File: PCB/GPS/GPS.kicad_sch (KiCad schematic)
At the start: 33 parts, among them J1 DC, J2 USB-C, J3 Shelly, J4 Conn_01x05_Male, J5 Conn_01x05_Male, U1 L86-M33, U2 ESP32-PICO-MINI-02, U3 FT231XQ, U4 LMR16006+FB, U5 QR

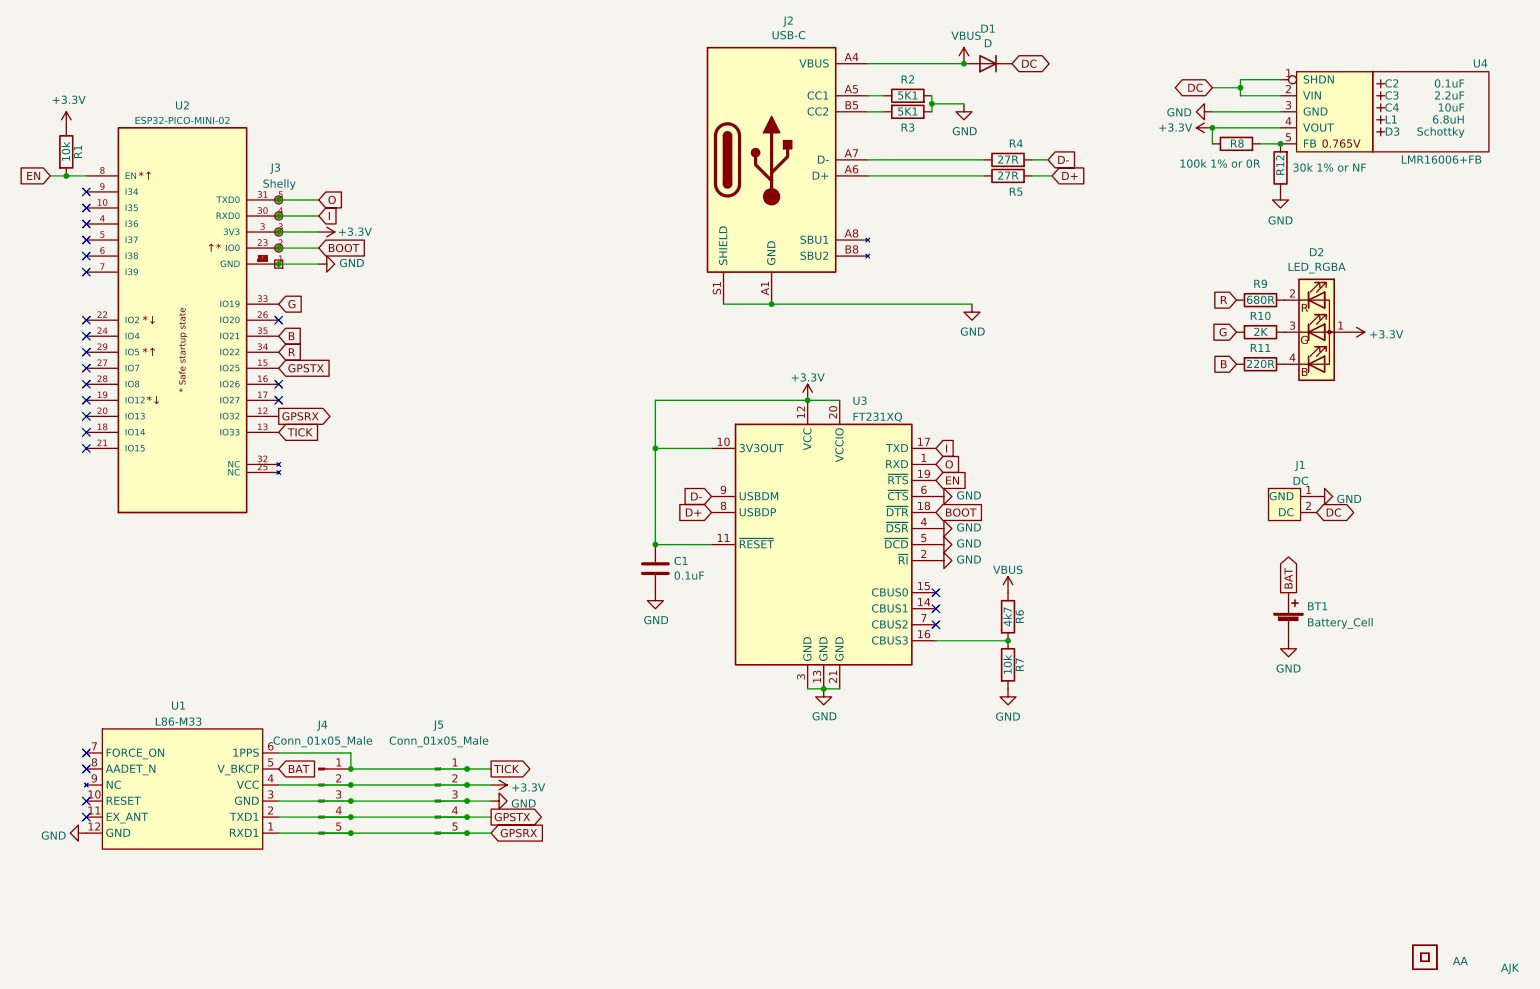
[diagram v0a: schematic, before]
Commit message: Changed GPS to plug in module - will work with Generic when re-done
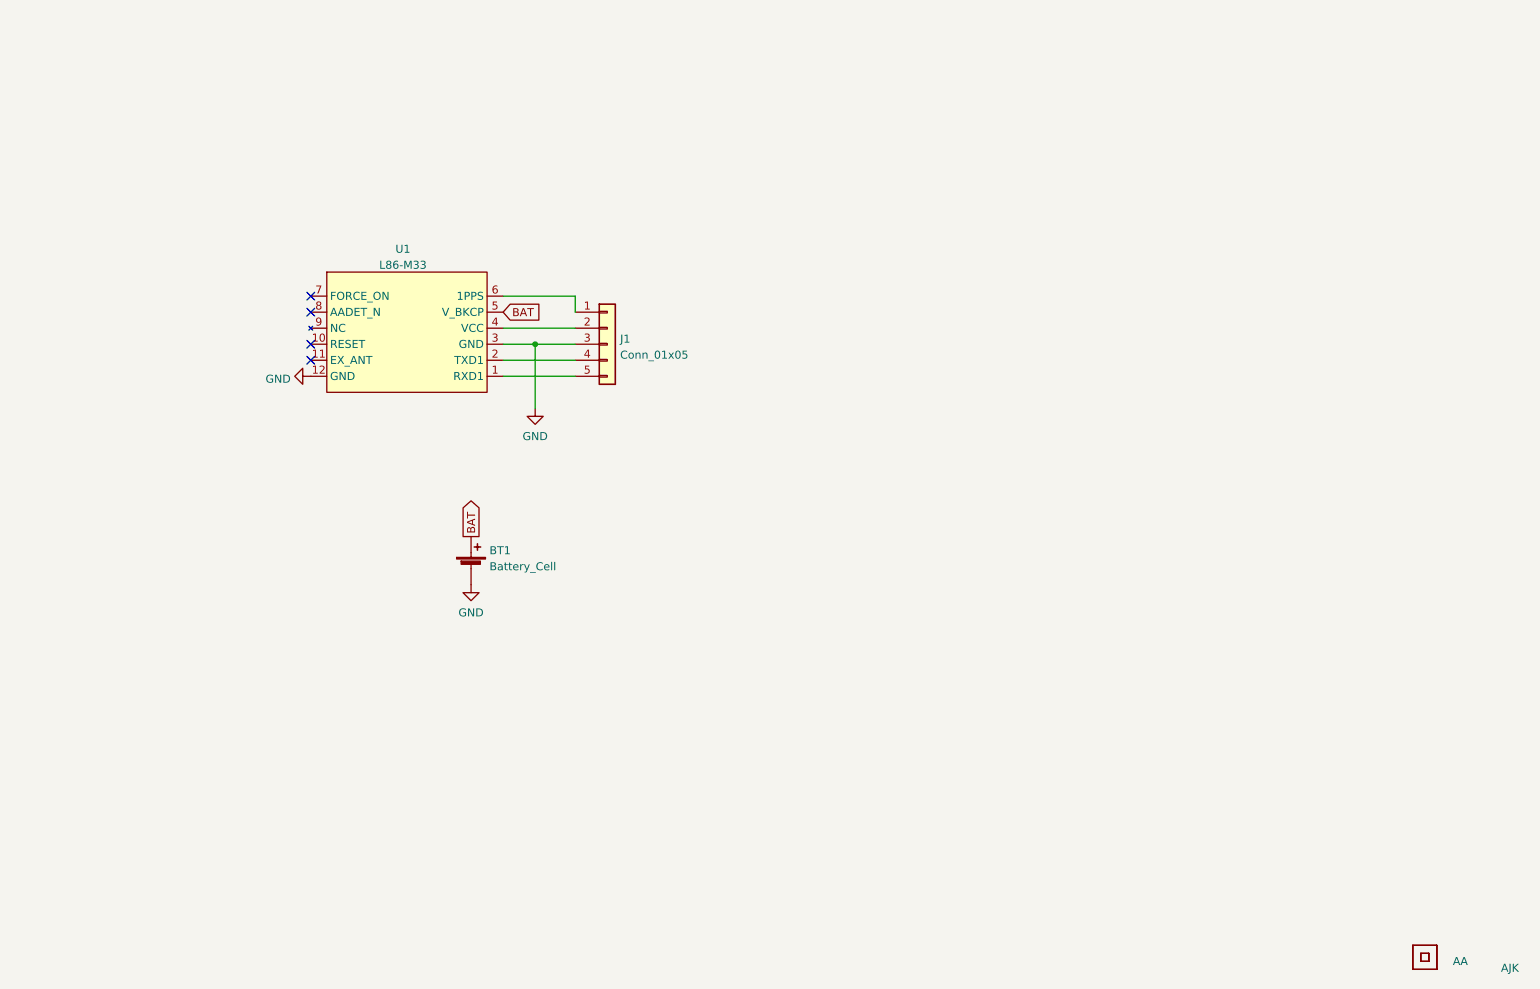
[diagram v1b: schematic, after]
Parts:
- removed C1: 0.1uF, RevK:C_0603, symbol Device:C
- removed C2: 0.1uF, RevK:C_0603_, symbol RevK:Hidden
- removed C3: 2.2uF, RevK:C_0805_, symbol RevK:Hidden
- removed C4: 10uF, RevK:C_0805_, symbol RevK:Hidden
- removed D1: D, RevK:D_1206, symbol Device:D
- removed D2: LED_RGBA, RevK:LED-RGB-1.6x1.6, symbol Device:LED_ARGB
- removed D3: Schottky, RevK:D_1206_, symbol RevK:Hidden
- removed J1: DC, RevK:Molex_MiniSPOX_H2RA, symbol RevK:DC
- removed J2: USB-C, RevK:USC16-TR, symbol RevK:USB-C
- removed J3: Shelly, RevK:Shelly, symbol RevK:Shelly
- removed J4, J5: Conn_01x05_Male, Connector_PinHeader_1.27mm:PinHeader_1x05_P1.27mm_Vertical, symbol Connector:Conn_01x05_Male
- removed L1: 6.8uH, RevK:L_4x4_, symbol RevK:Hidden
- removed R1, R7: 10k, RevK:R_0603, symbol Device:R
- removed R10: 2K, RevK:R_0603, symbol Device:R
- removed R11: 220R, RevK:R_0603, symbol Device:R
- removed R12: 30k 1% or NF, RevK:R_0603, symbol Device:R
- removed R2, R3: 5K1, RevK:R_0603, symbol Device:R
- removed R4, R5: 27R, RevK:R_0603, symbol Device:R
- removed R6: 4k7, RevK:R_0603, symbol Device:R
- removed R8: 100k 1% or 0R, RevK:R_0603, symbol Device:R
- removed R9: 680R, RevK:R_0603, symbol Device:R
- removed U2: ESP32-PICO-MINI-02, RevK:ESP32-PICO-MINI-02, symbol RevK:ESP32-PICO-MINI-02
- removed U3: FT231XQ, RevK:QFN-20-1EP_4x4mm_P0.5mm_EP2.5x2.5mm, symbol RevK:FT231XQ
- removed U4: LMR16006+FB, RevK:SOT-23-Thin-6-Reg, symbol RevK:LMR16006+FB
- added J1: Conn_01x05, RevK:PTSM-HH-5-RA-P, symbol Connector_Generic:Conn_01x05
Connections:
- net GND: now also J1.3 (Pin_3)
- net +3V3: no longer names the net of U1.4 (VCC)
- net +3V3: now also J1.2 (Pin_2)
- net GPSRX: no longer names the net of U1.1 (RXD1)
- net GPSRX: now also J1.5 (Pin_5)
- net GPSTX: no longer names the net of U1.2 (TXD1)
- net GPSTX: now also J1.4 (Pin_4)
- net TICK: no longer names the net of U1.6 (1PPS)
- net TICK: now also J1.1 (Pin_1)
- no-connect marks 25 -> 4
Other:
- moved on the sheet: BT1, U1

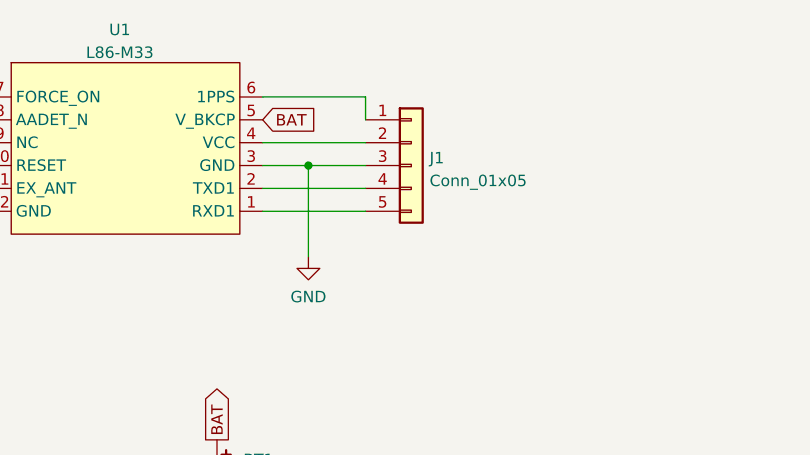
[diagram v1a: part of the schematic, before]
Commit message: New connectors, and separate GPS
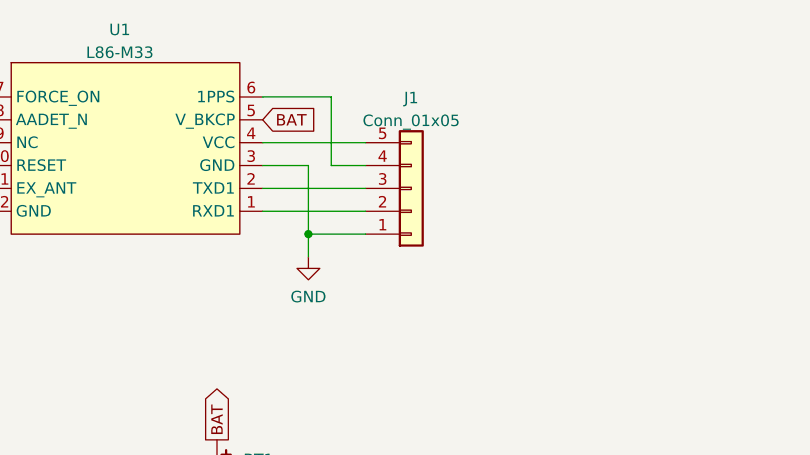
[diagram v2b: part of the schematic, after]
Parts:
- J1: footprint RevK:PTSM-HH-5-RA-P -> RevK:PTSM-HH-5-RA-P-SMD
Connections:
- net GND: now also J1.1 (Pin_1); no longer J1.3 (Pin_3)
- net at U1.6 (1PPS): now also J1.4 (Pin_4); no longer J1.1 (Pin_1)
- net at J1.2 (Pin_2): now also U1.1 (RXD1); no longer U1.4 (VCC)
- net at U1.2 (TXD1): now also J1.3 (Pin_3); no longer J1.4 (Pin_4)
- net at J1.5 (Pin_5): now also U1.4 (VCC); no longer U1.1 (RXD1)
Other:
- moved on the sheet: J1
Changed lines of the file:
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@@
     (comment 2 "www.me.uk")
   )
-  (junction (at 121.92 74.93) (diameter 0) (color 0 0 0 0)
+  (junction (at 121.92 82.55) (diameter 0) (color 0 0 0 0)
   )
   (no_connect (at 86.36 67.31))
@@
     (stroke (width 0) (type default) (color 0 0 0 0))
   )
-  (wire (pts (xy 121.92 74.93) (xy 121.92 85.09))
-    (stroke (width 0) (type default) (color 0 0 0 0))
-  )
-  (wire (pts (xy 116.84 67.31) (xy 128.27 67.31))
+  (wire (pts (xy 121.92 74.93) (xy 121.92 82.55))
+    (stroke (width 0) (type default) (color 0 0 0 0))
+  )
+  (wire (pts (xy 116.84 67.31) (xy 124.46 67.31))
     (stroke (width 0) (type default) (color 0 0 0 0))
   )
@@
     (stroke (width 0) (type default) (color 0 0 0 0))
   )
-  (wire (pts (xy 121.92 74.93) (xy 128.27 74.93))
+  (wire (pts (xy 124.46 67.31) (xy 124.46 74.93))
     (stroke (width 0) (type default) (color 0 0 0 0))
   )
@@
     (stroke (width 0) (type default) (color 0 0 0 0))
   )
-  (wire (pts (xy 128.27 67.31) (xy 128.27 69.85))
+  (wire (pts (xy 121.92 82.55) (xy 121.92 85.09))
+    (stroke (width 0) (type default) (color 0 0 0 0))
+  )
+  (wire (pts (xy 121.92 82.55) (xy 128.27 82.55))
+    (stroke (width 0) (type default) (color 0 0 0 0))
+  )
+  (wire (pts (xy 124.46 74.93) (xy 128.27 74.93))
     (stroke (width 0) (type default) (color 0 0 0 0))
   )
@@
     )
   )
-  (symbol (lib_id "Connector_Generic:Conn_01x05") (at 133.35 74.93 0) (unit 1)
-    (in_bom yes) (on_board yes) (fields_autoplaced)
-    (property "Reference" "J1" (id 0) (at 135.382 74.0953 0)
-      (effects (font (size 1.27 1.27)) (justify left))
-    )
-    (property "Value" "Conn_01x05" (id 1) (at 135.382 76.6322 0)
-      (effects (font (size 1.27 1.27)) (justify left))
-    )
-    (property "Footprint" "RevK:PTSM-HH-5-RA-P" (id 2) (at 133.35 74.93 0)
-      (effects (font (size 1.27 1.27)) hide)
-    )
-    (property "Datasheet" "~" (id 3) (at 133.35 74.93 0)
+  (symbol (lib_id "Connector_Generic:Conn_01x05") (at 133.35 77.47 0) (mirror x) (unit 1)
+    (in_bom yes) (on_board yes) (fields_autoplaced)
+    (property "Reference" "J1" (id 0) (at 133.35 67.4202 0))
+    (property "Value" "Conn_01x05" (id 1) (at 133.35 69.9571 0))
+    (property "Footprint" "RevK:PTSM-HH-5-RA-P-SMD" (id 2) (at 133.35 77.47 0)
+      (effects (font (size 1.27 1.27)) hide)
+    )
+    (property "Datasheet" "~" (id 3) (at 133.35 77.47 0)
       (effects (font (size 1.27 1.27)) hide)
     )
@@
     )
     (path "/85d5bf86-3b25-4dba-8dc2-950cbe3c82ce"
-      (reference "J1") (unit 1) (value "Conn_01x05") (footprint "RevK:PTSM-HH-5-RA-P")
+      (reference "J1") (unit 1) (value "Conn_01x05") (footprint "RevK:PTSM-HH-5-RA-P-SMD")
     )
     (path "/00000000-0000-0000-0000-000060b9351c"

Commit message: Clean up
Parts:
- J1: Phenoix part (none) -> 1814948
